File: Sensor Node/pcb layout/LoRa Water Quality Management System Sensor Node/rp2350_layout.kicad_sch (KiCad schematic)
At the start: 28 parts, among them J10 Conn_01x03, J9 Conn_01x02, U7 W25Q128JVSIQ TR, U8 RP2350_60QFN, Y1 ABM8-272-T3

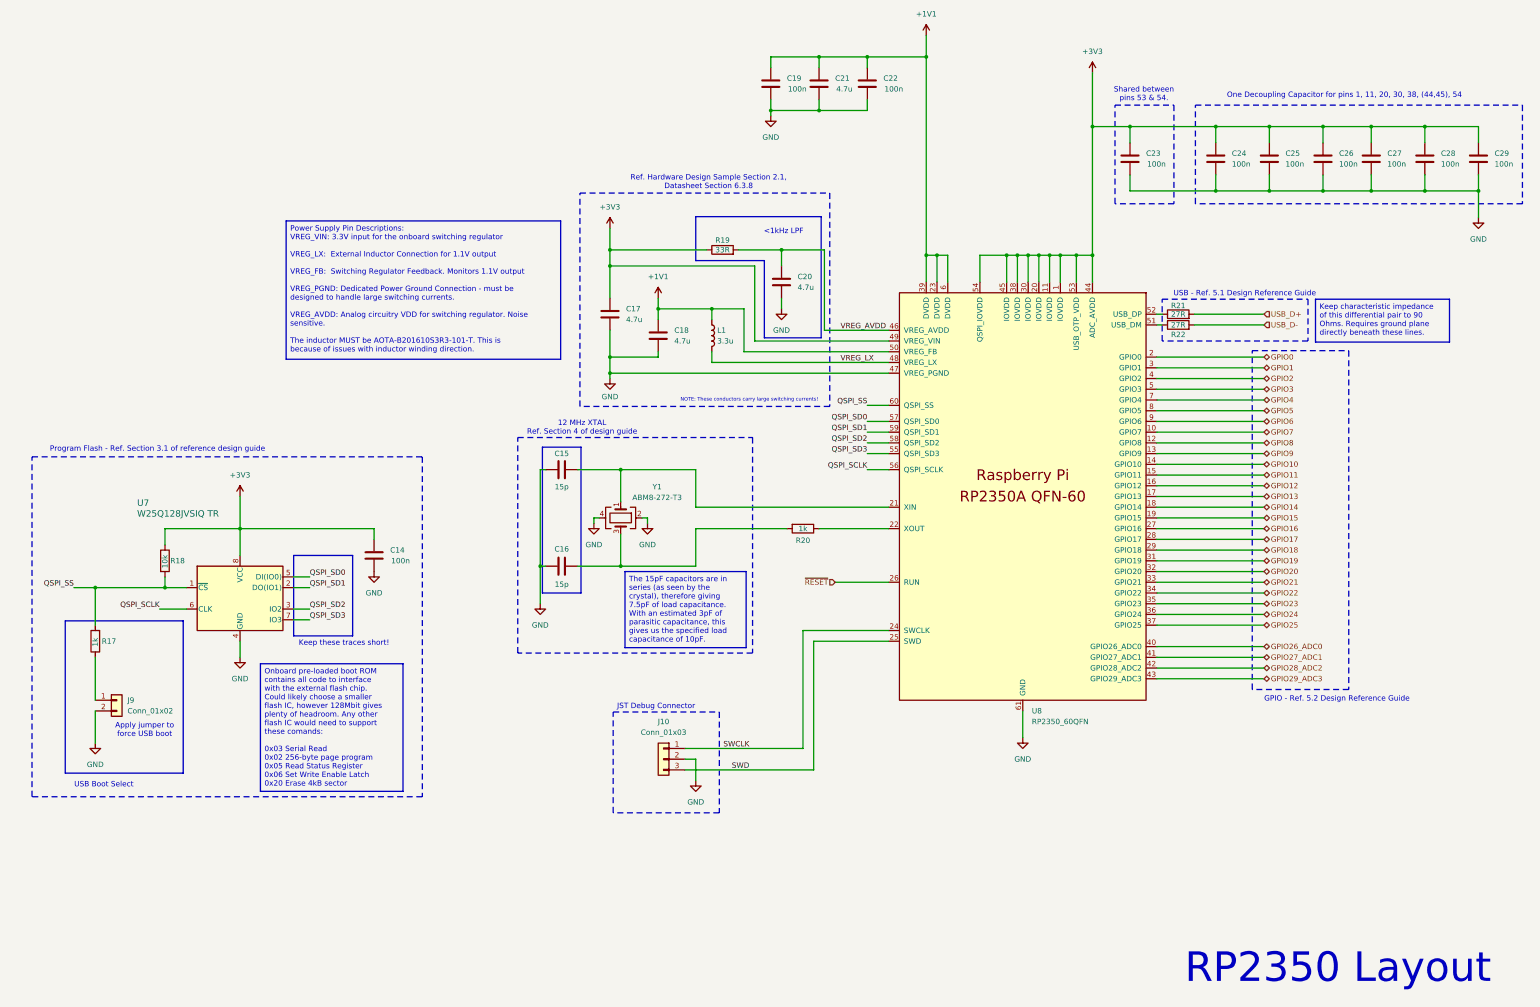
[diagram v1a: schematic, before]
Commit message: Add PCB "B" variant, which uses INA333 and LMV321 instead of discrete instrumentation amplifier.
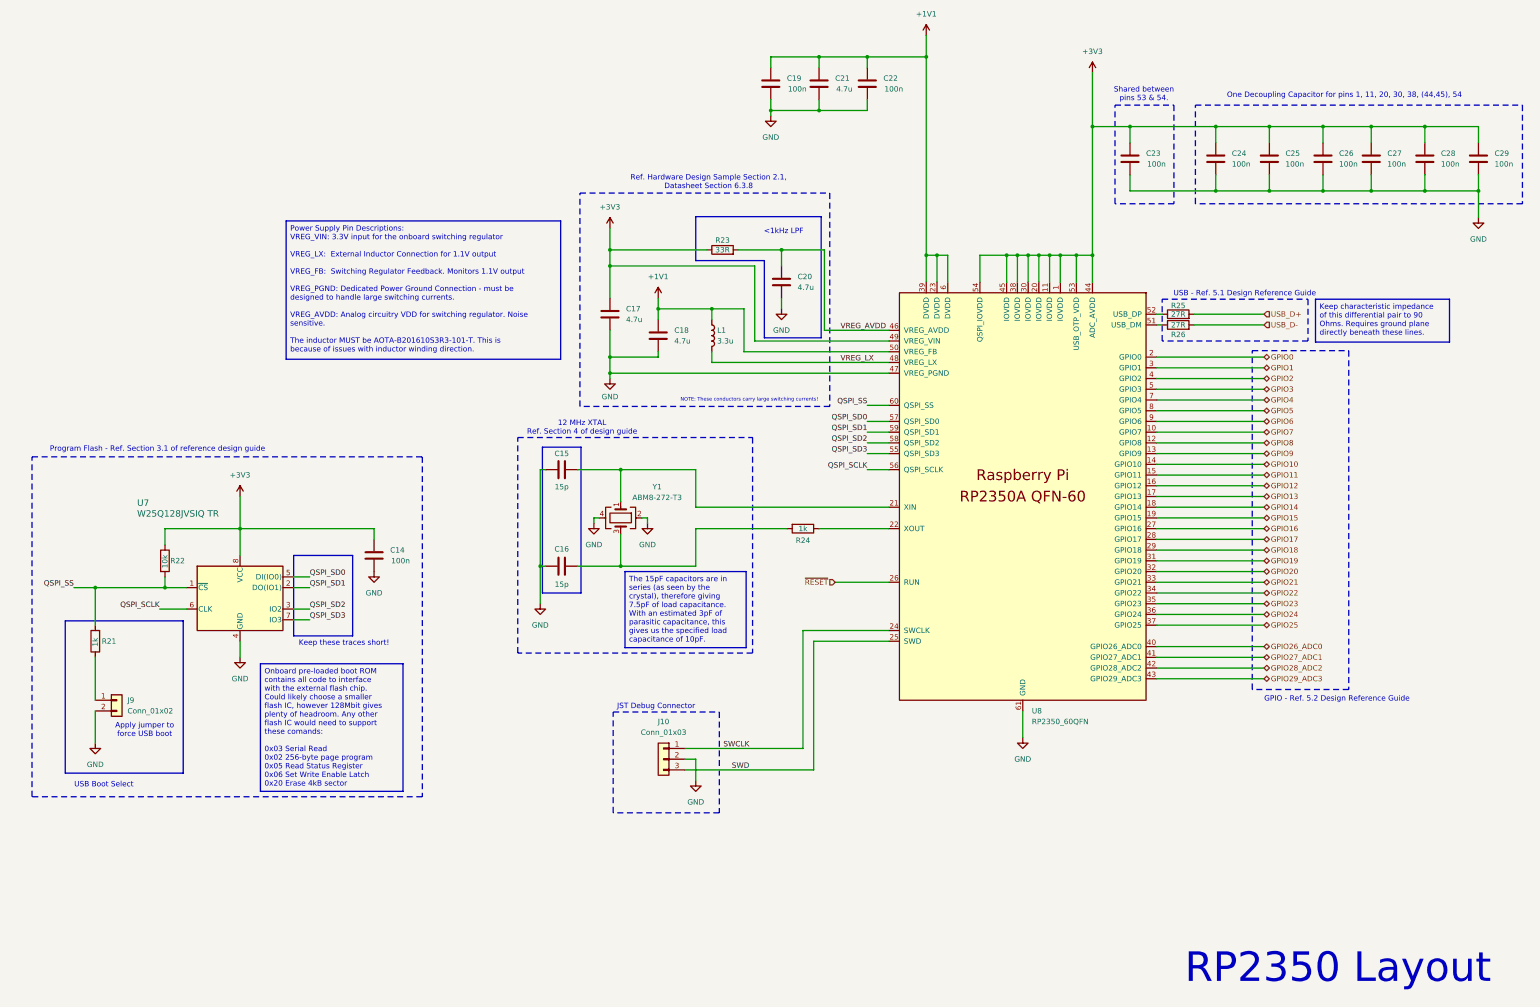
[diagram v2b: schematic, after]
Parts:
- renumbered R17 to R21, R18 to R22, R19 to R23, R20 to R24, R21 to R25, R22 to R26
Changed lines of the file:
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@@
 		(dnp no)
 		(fields_autoplaced yes)
-		(property "Reference" "#PWR050"
+		(property "Reference" "#PWR056"
 			(at 190.5 223.52 0)
 			(effects
@@
 			(project ""
 				(path "/f090528b-8c52-4bf9-a2b8-0c17aa5e5727/8ed505b3-7460-4c84-b5db-8c51c81aa9b0"
-					(reference "#PWR050")
+					(reference "#PWR056")
 					(unit 1)
 				)
@@
 		(dnp no)
 		(fields_autoplaced yes)
-		(property "Reference" "#PWR048"
+		(property "Reference" "#PWR054"
 			(at 179.07 162.56 0)
 			(effects
@@
 			(project ""
 				(path "/f090528b-8c52-4bf9-a2b8-0c17aa5e5727/8ed505b3-7460-4c84-b5db-8c51c81aa9b0"
-					(reference "#PWR048")
+					(reference "#PWR054")
 					(unit 1)
 				)
@@
 		(dnp no)
 		(fields_autoplaced yes)
-		(property "Reference" "#PWR051"
+		(property "Reference" "#PWR057"
 			(at 208.28 66.04 0)
 			(effects
@@
 			(project ""
 				(path "/f090528b-8c52-4bf9-a2b8-0c17aa5e5727/8ed505b3-7460-4c84-b5db-8c51c81aa9b0"
-					(reference "#PWR051")
+					(reference "#PWR057")
 					(unit 1)
 				)
@@
 		(dnp no)
 		(fields_autoplaced yes)
-		(property "Reference" "#PWR042"
+		(property "Reference" "#PWR048"
 			(at 82.55 194.31 0)
 			(effects
@@
 			(project "LoRa Water Quality Management System Sensor Node"
 				(path "/f090528b-8c52-4bf9-a2b8-0c17aa5e5727/8ed505b3-7460-4c84-b5db-8c51c81aa9b0"
-					(reference "#PWR042")
+					(reference "#PWR048")
 					(unit 1)
 				)
@@
 		(dnp no)
 		(fields_autoplaced yes)
-		(property "Reference" "#PWR052"
+		(property "Reference" "#PWR058"
 			(at 210.82 111.76 0)
 			(effects
@@
 			(project ""
 				(path "/f090528b-8c52-4bf9-a2b8-0c17aa5e5727/8ed505b3-7460-4c84-b5db-8c51c81aa9b0"
-					(reference "#PWR052")
+					(reference "#PWR058")
 					(unit 1)
 				)
@@
 		(dnp no)
 		(fields_autoplaced yes)
-		(property "Reference" "#PWR056"
+		(property "Reference" "#PWR062"
 			(at 375.92 90.17 0)
 			(effects
@@
 			(project ""
 				(path "/f090528b-8c52-4bf9-a2b8-0c17aa5e5727/8ed505b3-7460-4c84-b5db-8c51c81aa9b0"
-					(reference "#PWR056")
+					(reference "#PWR062")
 					(unit 1)
 				)
@@
 		(dnp no)
 		(fields_autoplaced yes)
-		(property "Reference" "#PWR053"
+		(property "Reference" "#PWR059"
 			(at 245.11 44.45 0)
 			(effects
@@
 			(project "LoRa Water Quality Management System Sensor Node"
 				(path "/f090528b-8c52-4bf9-a2b8-0c17aa5e5727/8ed505b3-7460-4c84-b5db-8c51c81aa9b0"
-					(reference "#PWR053")
+					(reference "#PWR059")
 					(unit 1)
 				)
@@
 		(on_board yes)
 		(dnp no)
-		(property "Reference" "#PWR047"
+		(property "Reference" "#PWR053"
 			(at 170.18 128.27 0)
 			(effects
@@
 			(project ""
 				(path "/f090528b-8c52-4bf9-a2b8-0c17aa5e5727/8ed505b3-7460-4c84-b5db-8c51c81aa9b0"
-					(reference "#PWR047")
+					(reference "#PWR053")
 					(unit 1)
 				)
@@
 		(dnp no)
 		(fields_autoplaced yes)
-		(property "Reference" "#PWR045"
+		(property "Reference" "#PWR051"
 			(at 166.37 162.56 0)
 			(effects
@@
 			(project "LoRa Water Quality Management System Sensor Node"
 				(path "/f090528b-8c52-4bf9-a2b8-0c17aa5e5727/8ed505b3-7460-4c84-b5db-8c51c81aa9b0"
-					(reference "#PWR045")
+					(reference "#PWR051")
 					(unit 1)
 				)
@@
 		(on_board yes)
 		(dnp no)
-		(property "Reference" "R17"
+		(property "Reference" "R21"
 			(at 49.784 184.15 0)
 			(effects
@@
 			(project ""
 				(path "/f090528b-8c52-4bf9-a2b8-0c17aa5e5727/8ed505b3-7460-4c84-b5db-8c51c81aa9b0"
-					(reference "R17")
+					(reference "R21")
 					(unit 1)
 				)
@@
 		(on_board yes)
 		(dnp no)
-		(property "Reference" "R18"
+		(property "Reference" "R22"
 			(at 66.04 165.1 0)
 			(effects
@@
 			(project ""
 				(path "/f090528b-8c52-4bf9-a2b8-0c17aa5e5727/8ed505b3-7460-4c84-b5db-8c51c81aa9b0"
-					(reference "R18")
+					(reference "R22")
 					(unit 1)
 				)
@@
 		(dnp no)
 		(fields_autoplaced yes)
-		(property "Reference" "#PWR040"
+		(property "Reference" "#PWR046"
 			(at 48.26 214.63 0)
 			(effects
@@
 			(project ""
 				(path "/f090528b-8c52-4bf9-a2b8-0c17aa5e5727/8ed505b3-7460-4c84-b5db-8c51c81aa9b0"
-					(reference "#PWR040")
+					(reference "#PWR046")
 					(unit 1)
 				)
@@
 		(on_board yes)
 		(dnp no)
-		(property "Reference" "R22"
+		(property "Reference" "R26"
 			(at 304.8 111.506 90)
 			(effects
@@
 			(project "LoRa Water Quality Management System Sensor Node"
 				(path "/f090528b-8c52-4bf9-a2b8-0c17aa5e5727/8ed505b3-7460-4c84-b5db-8c51c81aa9b0"
-					(reference "R22")
+					(reference "R26")
 					(unit 1)
 				)
@@
 		(dnp no)
 		(fields_autoplaced yes)
-		(property "Reference" "#PWR041"
+		(property "Reference" "#PWR047"
 			(at 82.55 153.67 0)
 			(effects
@@
 			(project ""
 				(path "/f090528b-8c52-4bf9-a2b8-0c17aa5e5727/8ed505b3-7460-4c84-b5db-8c51c81aa9b0"
-					(reference "#PWR041")
+					(reference "#PWR047")
 					(unit 1)
 				)
@@
 		(on_board yes)
 		(dnp no)
-		(property "Reference" "R21"
+		(property "Reference" "R25"
 			(at 304.8 104.648 90)
 			(effects
@@
 			(project ""
 				(path "/f090528b-8c52-4bf9-a2b8-0c17aa5e5727/8ed505b3-7460-4c84-b5db-8c51c81aa9b0"
-					(reference "R21")
+					(reference "R25")
 					(unit 1)
 				)
@@
 		(dnp no)
 		(fields_autoplaced yes)
-		(property "Reference" "#PWR043"
+		(property "Reference" "#PWR049"
 			(at 114.3 173.99 0)
 			(effects
@@
 			(project "LoRa Water Quality Management System Sensor Node"
 				(path "/f090528b-8c52-4bf9-a2b8-0c17aa5e5727/8ed505b3-7460-4c84-b5db-8c51c81aa9b0"
-					(reference "#PWR043")
+					(reference "#PWR049")
 					(unit 1)
 				)
@@
 		(dnp no)
 		(fields_autoplaced yes)
-		(property "Reference" "#PWR055"
+		(property "Reference" "#PWR061"
 			(at 284.48 53.34 0)
 			(effects
@@
 			(project ""
 				(path "/f090528b-8c52-4bf9-a2b8-0c17aa5e5727/8ed505b3-7460-4c84-b5db-8c51c81aa9b0"
-					(reference "#PWR055")
+					(reference "#PWR061")
 					(unit 1)
 				)
@@
 		(on_board yes)
 		(dnp no)
-		(property "Reference" "R19"
+		(property "Reference" "R23"
 			(at 196.85 89.154 90)
 			(effects
@@
 			(project ""
 				(path "/f090528b-8c52-4bf9-a2b8-0c17aa5e5727/8ed505b3-7460-4c84-b5db-8c51c81aa9b0"
-					(reference "R19")
+					(reference "R23")
 					(unit 1)
 				)
@@
 		(dnp no)
 		(fields_autoplaced yes)
-		(property "Reference" "#PWR054"
+		(property "Reference" "#PWR060"
 			(at 267.97 213.36 0)
 			(effects
@@
 			(project ""
 				(path "/f090528b-8c52-4bf9-a2b8-0c17aa5e5727/8ed505b3-7460-4c84-b5db-8c51c81aa9b0"
-					(reference "#PWR054")
+					(reference "#PWR060")
 					(unit 1)
 				)
@@
 		(on_board yes)
 		(dnp no)
-		(property "Reference" "R20"
+		(property "Reference" "R24"
 			(at 215.9 160.274 90)
 			(effects
@@
 			(project "LoRa Water Quality Management System Sensor Node"
 				(path "/f090528b-8c52-4bf9-a2b8-0c17aa5e5727/8ed505b3-7460-4c84-b5db-8c51c81aa9b0"
-					(reference "R20")
+					(reference "R24")
 					(unit 1)
 				)
@@
 		(dnp no)
 		(fields_autoplaced yes)
-		(property "Reference" "#PWR049"
+		(property "Reference" "#PWR055"
 			(at 181.61 106.68 0)
 			(effects
@@
 			(project ""
 				(path "/f090528b-8c52-4bf9-a2b8-0c17aa5e5727/8ed505b3-7460-4c84-b5db-8c51c81aa9b0"
-					(reference "#PWR049")
+					(reference "#PWR055")
 					(unit 1)
 				)
@@
 		(dnp no)
 		(fields_autoplaced yes)
-		(property "Reference" "#PWR046"
+		(property "Reference" "#PWR052"
 			(at 170.18 90.17 0)
 			(effects
@@
 			(project ""
 				(path "/f090528b-8c52-4bf9-a2b8-0c17aa5e5727/8ed505b3-7460-4c84-b5db-8c51c81aa9b0"
-					(reference "#PWR046")
+					(reference "#PWR052")
 					(unit 1)
 				)
@@
 		(dnp no)
 		(fields_autoplaced yes)
-		(property "Reference" "#PWR044"
+		(property "Reference" "#PWR050"
 			(at 153.67 181.61 0)
 			(effects
@@
 			(project "LoRa Water Quality Management System Sensor Node"
 				(path "/f090528b-8c52-4bf9-a2b8-0c17aa5e5727/8ed505b3-7460-4c84-b5db-8c51c81aa9b0"
-					(reference "#PWR044")
-					(unit 1)
-				)
+					(reference "#PWR050")
+					(unit 1)
+				)
